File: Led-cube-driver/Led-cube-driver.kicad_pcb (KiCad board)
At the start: 2 copper layers, 31 parts, among them J1 Diodes-input, J2 Vin, J3 Diodes-output, J4 Layers-input, J5 Layers-output, Q1 BC547, Q2 BC547, Q3 BC547, Q4 BC547, U1 74HC164, U2 74HC164

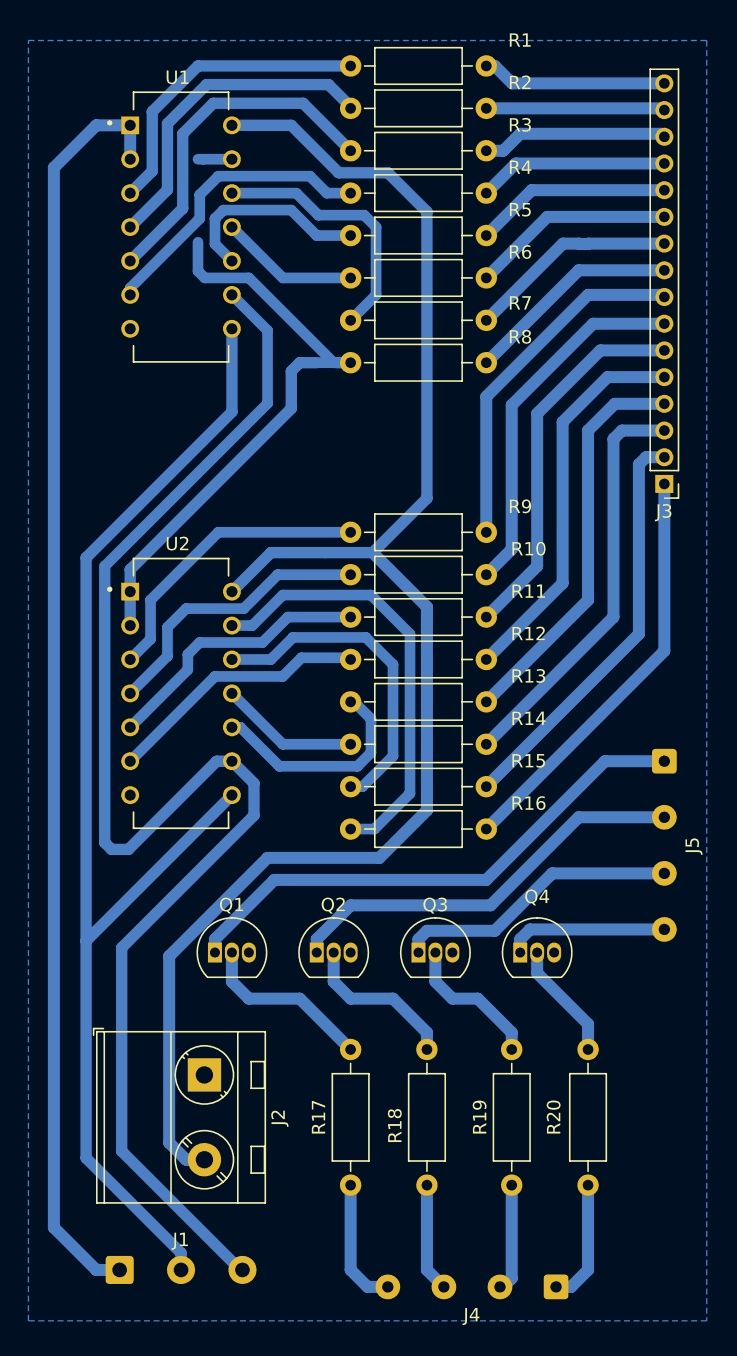
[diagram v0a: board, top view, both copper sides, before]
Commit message: led driver update
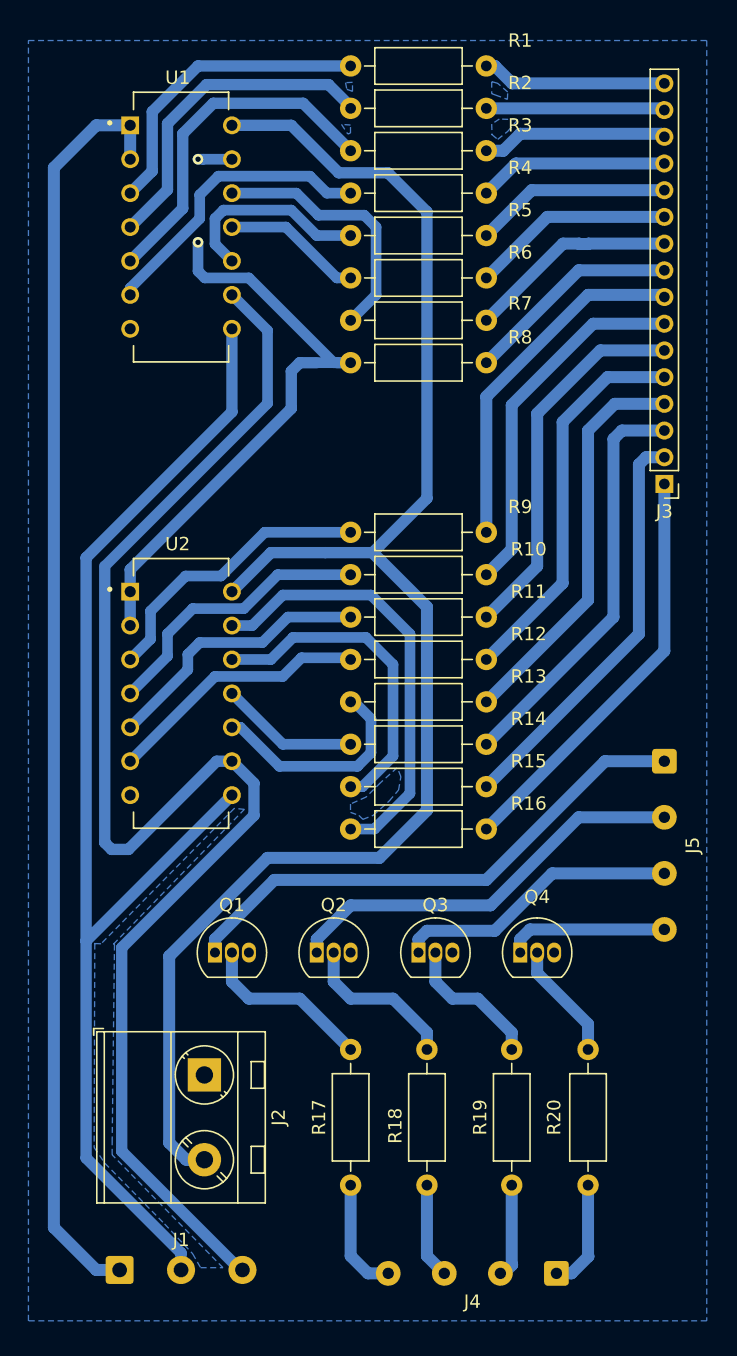
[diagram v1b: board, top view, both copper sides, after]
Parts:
- moved J4 1.02 mm to (131.6, 157.1)
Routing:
- net Net-(J4-Pad1): track 9.27 -> 8.27 mm
- net Net-(J4-Pad4): track 9.66 -> 8.66 mm
- net Net-(J4-Pad3): track 8.15 -> 7.14 mm
- net Net-(J4-Pad2): track 8.13 -> 7.13 mm
- net Net-(R8-Pad1): vias 0 -> 2
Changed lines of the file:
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@@
   )
   (footprint "Connector_Wire:SolderWire-0.25sqmm_1x04_P4.2mm_D0.65mm_OD1.7mm" (layer "F.Cu")
-    (at 131.59 158.115 180)
+    (at 131.62 157.1 180)
     (descr "Soldered wire connection, for 4 times 0.25 mm² wires, basic insulation, conductor diameter 0.65mm, outer diameter 1.7mm, size source Multi-Contact FLEXI-E_0.25 (https://ec.staubli.com/AcroFiles/Catalogues/TM_Cab-Main-11014119_(en)_hi.pdf), bend radius 3 times outer diameter, generated with kicad-footprint-generator")
     (tags "connector wire 0.25sqmm")
@@
   (segment (start 134.016 79.979) (end 139.7 79.979) (width 0.9) (layer "B.Cu") (net 4))
   (segment (start 126.365 85.725) (end 132.111 79.979) (width 0.9) (layer "B.Cu") (net 4))
-  (segment (start 131.59 158.115) (end 132.715 158.115) (width 0.9) (layer "B.Cu") (net 5))
-  (segment (start 133.985 156.845) (end 133.985 150.495) (width 0.9) (layer "B.Cu") (net 5))
-  (segment (start 132.715 158.115) (end 133.985 156.845) (width 0.9) (layer "B.Cu") (net 5))
+  (segment (start 131.62 157.1) (end 132.745 157.1) (width 0.9) (layer "B.Cu") (net 5))
+  (segment (start 134.015 155.83) (end 133.985 155.8) (width 0.9) (layer "B.Cu") (net 5))
+  (segment (start 133.985 155.8) (end 133.985 150.495) (width 0.9) (layer "B.Cu") (net 5))
+  (segment (start 132.745 157.1) (end 134.015 155.83) (width 0.9) (layer "B.Cu") (net 5))
   (segment (start 133.985 140.335) (end 133.985 138.43) (width 0.9) (layer "B.Cu") (net 6))
   (segment (start 133.985 138.43) (end 130.175 134.62) (width 0.9) (layer "B.Cu") (net 6))
   (segment (start 130.175 134.62) (end 130.175 133.075) (width 0.9) (layer "B.Cu") (net 6))
-  (segment (start 128.27 157.48) (end 128.27 150.495) (width 0.9) (layer "B.Cu") (net 7))
-  (segment (start 127.39 158.115) (end 127.635 158.115) (width 0.9) (layer "B.Cu") (net 7))
-  (segment (start 127.635 158.115) (end 128.27 157.48) (width 0.9) (layer "B.Cu") (net 7))
+  (segment (start 128.3 156.465) (end 128.27 156.435) (width 0.9) (layer "B.Cu") (net 7))
+  (segment (start 127.42 157.1) (end 127.665 157.1) (width 0.9) (layer "B.Cu") (net 7))
+  (segment (start 127.665 157.1) (end 128.3 156.465) (width 0.9) (layer "B.Cu") (net 7))
+  (segment (start 128.27 156.435) (end 128.27 150.495) (width 0.9) (layer "B.Cu") (net 7))
   (segment (start 123.825 136.525) (end 122.555 135.255) (width 0.9) (layer "B.Cu") (net 8))
   (segment (start 125.73 136.525) (end 123.825 136.525) (width 0.9) (layer "B.Cu") (net 8))
@@
   (segment (start 122.555 135.255) (end 122.555 133.075) (width 0.9) (layer "B.Cu") (net 8))
   (segment (start 128.27 139.065) (end 125.73 136.525) (width 0.9) (layer "B.Cu") (net 8))
-  (segment (start 121.92 156.845) (end 121.92 150.495) (width 0.9) (layer "B.Cu") (net 9))
-  (segment (start 123.19 158.115) (end 121.92 156.845) (width 0.9) (layer "B.Cu") (net 9))
+  (segment (start 121.92 155.8) (end 121.92 150.495) (width 0.9) (layer "B.Cu") (net 9))
+  (segment (start 123.22 157.1) (end 121.92 155.8) (width 0.9) (layer "B.Cu") (net 9))
   (segment (start 116.205 136.525) (end 114.935 135.255) (width 0.9) (layer "B.Cu") (net 10))
   (segment (start 121.92 139.065) (end 119.38 136.525) (width 0.9) (layer "B.Cu") (net 10))
@@
   (segment (start 121.92 140.335) (end 121.92 139.065) (width 0.9) (layer "B.Cu") (net 10))
   (segment (start 114.935 135.255) (end 114.935 133.075) (width 0.9) (layer "B.Cu") (net 10))
-  (segment (start 117.475 158.115) (end 116.205 156.845) (width 0.9) (layer "B.Cu") (net 11))
-  (segment (start 116.205 156.845) (end 116.205 150.495) (width 0.9) (layer "B.Cu") (net 11))
-  (segment (start 118.99 158.115) (end 117.475 158.115) (width 0.9) (layer "B.Cu") (net 11))
+  (segment (start 116.205 155.8) (end 116.205 150.495) (width 0.9) (layer "B.Cu") (net 11))
+  (segment (start 119.02 157.1) (end 117.505 157.1) (width 0.9) (layer "B.Cu") (net 11))
+  (segment (start 117.505 157.1) (end 116.205 155.8) (width 0.9) (layer "B.Cu") (net 11))
   (segment (start 116.205 140.335) (end 112.395 136.525) (width 0.9) (layer "B.Cu") (net 12))
   (segment (start 112.395 136.525) (end 108.585 136.525) (width 0.9) (layer "B.Cu") (net 12))
@@
   (segment (start 130.175 104.14) (end 130.175 92.71) (width 0.9) (layer "B.Cu") (net 24))
   (segment (start 126.365 107.95) (end 130.175 104.14) (width 0.9) (layer "B.Cu") (net 24))
+  (segment (start 104.38 107.315) (end 108.204 107.315) (width 0.8) (layer "B.Cu") (net 25))
+  (segment (start 102.489 109.206) (end 104.38 107.315) (width 0.8) (layer "B.Cu") (net 25))
+  (segment (start 108.204 107.315) (end 110.744 104.775) (width 0.8) (layer "B.Cu") (net 25))
+  (segment (start 102.489 110.871) (end 102.489 109.206) (width 0.8) (layer "B.Cu") (net 25))
   (segment (start 99.695 113.665) (end 102.489 110.871) (width 0.8) (layer "B.Cu") (net 25))
   (segment (start 110.744 104.775) (end 116.205 104.775) (width 0.8) (layer "B.Cu") (net 25))
-  (segment (start 102.489 110.871) (end 102.489 108.712) (width 0.8) (layer "B.Cu") (net 25))
-  (segment (start 102.489 108.712) (end 103.886 107.315) (width 0.8) (layer "B.Cu") (net 25))
-  (segment (start 103.886 107.315) (end 108.204 107.315) (width 0.8) (layer "B.Cu") (net 25))
-  (segment (start 108.204 107.315) (end 110.744 104.775) (width 0.8) (layer "B.Cu") (net 25))
   (segment (start 128.27 92.075) (end 134.366 85.979) (width 0.9) (layer "B.Cu") (net 26))
   (segment (start 126.365 104.775) (end 128.27 102.87) (width 0.9) (layer "B.Cu") (net 26))
   (segment (start 128.27 102.87) (end 128.27 92.075) (width 0.9) (layer "B.Cu") (net 26))
   (segment (start 134.366 85.979) (end 139.7 85.979) (width 0.9) (layer "B.Cu") (net 26))
+  (segment (start 106.495 104.875) (end 109.77 101.6) (width 0.8) (layer "B.Cu") (net 27))
+  (segment (start 109.77 101.6) (end 116.205 101.6) (width 0.8) (layer "B.Cu") (net 27))
+  (segment (start 103.845 104.875) (end 106.495 104.875) (width 0.8) (layer "B.Cu") (net 27))
   (segment (start 99.695 111.125) (end 101.219 109.601) (width 0.8) (layer "B.Cu") (net 27))
-  (segment (start 101.219 106.68) (end 106.299 101.6) (width 0.8) (layer "B.Cu") (net 27))
-  (segment (start 106.299 101.6) (end 116.205 101.6) (width 0.8) (layer "B.Cu") (net 27))
-  (segment (start 101.219 109.601) (end 101.219 106.68) (width 0.8) (layer "B.Cu") (net 27))
+  (segment (start 101.219 107.501) (end 103.845 104.875) (width 0.8) (layer "B.Cu") (net 27))
+  (segment (start 101.219 109.601) (end 101.219 107.501) (width 0.8) (layer "B.Cu") (net 27))
   (segment (start 133.985 83.82) (end 139.541 83.82) (width 0.9) (layer "B.Cu") (net 28))
   (segment (start 139.541 83.82) (end 139.7 83.979) (width 0.9) (layer "B.Cu") (net 28))
   (segment (start 126.365 101.6) (end 126.365 91.44) (width 0.9) (layer "B.Cu") (net 28))
   (segment (start 126.365 91.44) (end 133.985 83.82) (width 0.9) (layer "B.Cu") (net 28))
+  (via (at 104.775 73.66) (size 0.8) (drill 0.4) (layers "F.Cu" "B.Cu") (net 29))
+  (via (at 104.775 79.883) (size 0.8) (drill 0.4) (layers "F.Cu" "B.Cu") (net 29))
   (segment (start 115.189 88.9) (end 116.205 88.9) (width 0.85) (layer "B.Cu") (net 29))
   (segment (start 104.775 82.042) (end 104.775 79.883) (width 0.8) (layer "B.Cu") (net 29))
@@
   (segment (start 133.286 81.979) (end 139.7 81.979) (width 0.9) (layer "B.Cu") (net 30))
   (segment (start 126.365 88.9) (end 133.286 81.979) (width 0.9) (layer "B.Cu") (net 30))
-  (segment (start 111.125 82.55) (end 116.205 82.55) (width 0.8) (layer "B.Cu") (net 31))
-  (segment (start 107.315 78.74) (end 111.125 82.55) (width 0.8) (layer "B.Cu") (net 31))
+  (segment (start 115.17 82.55) (end 116.205 82.55) (width 0.8) (layer "B.Cu") (net 31))
+  (segment (start 111.36 78.74) (end 115.17 82.55) (width 0.8) (layer "B.Cu") (net 31))
+  (segment (start 107.315 78.74) (end 111.36 78.74) (width 0.8) (layer "B.Cu") (net 31))
   (segment (start 126.365 82.55) (end 130.936 77.979) (width 0.9) (layer "B.Cu") (net 32))
   (segment (start 130.936 77.979) (end 139.7 77.979) (width 0.9) (layer "B.Cu") (net 32))
@@
       )
     )
+    (polygon
+      (pts
+        (xy 97.514638 132.416488)
+        (xy 97.044916 132.400831)
+        (xy 97.045 132.375)
+        (xy 97.02 132.4)
+        (xy 97.044916 132.400831)
+        (xy 96.995 147.675)
+        (xy 97.795 148.85)
+        (xy 102.27 153.4)
+        (xy 104.37 155.625)
+        (xy 104.97 156.675)
+        (xy 106.645 156.675)
+        (xy 98.345 148.225)
+        (xy 98.345 147.3)
+        (xy 98.52 132.45)
+        (xy 98.441708 132.44739)
+        (xy 108.245 122.35)
+        (xy 107.495 122.275)
+      )
+    )
+    (polygon
+      (pts
+        (xy 118.445 120.35)
+        (xy 117.37 121.425)
+        (xy 116.195 121.95)
+        (xy 116.195 122.575)
+        (xy 116.82 122.8)
+        (xy 117.12 123.1)
+        (xy 117.895 122.8)
+        (xy 119.095 121.725)
+        (xy 119.795 120.9)
+        (xy 119.97 119.9)
+        (xy 119.695 119.225)
+      )
+    )
+    (polygon
+      (pts
+        (xy 126.77 71.025)
+        (xy 126.794219 71.8)
+        (xy 126.77 71.8)
+        (xy 126.794866 71.820722)
+        (xy 126.795 71.825)
+        (xy 126.795 71.820833)
+        (xy 127.22 72.175)
+        (xy 127.97 71.575)
+        (xy 128.72 70.7)
+        (xy 127.345 70.65)
+      )
+    )
+    (polygon
+      (pts
+        (xy 115.995 71.775)
+        (xy 116.195 71.7)
+        (xy 116.195 71.1)
+        (xy 115.52 71.05)
+      )
+    )
+    (polygon
+      (pts
+        (xy 126.77 68.75)
+        (xy 127.045 68.85)
+        (xy 127.945 69.175)
+        (xy 127.97 68.625)
+        (xy 127.22 67.975)
+        (xy 126.77 67.85)
+      )
+    )
+    (polygon
+      (pts
+        (xy 115.82 67.925)
+        (xy 115.92 68.425)
+        (xy 116.345 68.575)
+        (xy 116.345 67.9)
+      )
+    )

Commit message: done
done
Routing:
- net Net-(J1-Pad2): track 93.4 -> 94.3 mm
- net Net-(J1-Pad3): track 106.4 -> 105.5 mm
- net Net-(R8-Pad1): track 47.7 -> 47.0 mm
- net Net-(J1-Pad1): track 95.2 -> 95.7 mm

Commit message: newFiles
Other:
- board outline added: 51.2 x 96.1 mm
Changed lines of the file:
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@@
     (pad "14" thru_hole circle (at 3.81 -7.62) (size 1.338 1.338) (drill 0.83) (layers *.Cu *.Mask)
       (net 2 "VCC") (pinfunction "VCC") (pintype "power_in"))
+    (model "C:/Users/domin/Downloads/HEF4071BP.STEP"
+      (offset (xyz 0 0 0))
+      (scale (xyz 1 1 1))
+      (rotate (xyz -90 0 0))
+    )
   )
   (footprint "Package_TO_SOT_THT:TO-92_Inline" (layer "F.Cu")
@@
     (pad "2" thru_hole circle (at 6.35 0 270) (size 2.5 2.5) (drill 1.3) (layers *.Cu *.Mask)
       (net 2 "VCC") (pinfunction "Pin_2") (pintype "passive"))
-    (model "${KICAD6_3DMODEL_DIR}/TerminalBlock_MetzConnect.3dshapes/TerminalBlock_MetzConnect_Type701_RT11L02HGLU_1x02_P6.35mm_Horizontal.wrl"
-      (offset (xyz 0 0 0))
-      (scale (xyz 1 1 1))
-      (rotate (xyz 0 0 0))
-    )
   )
   (footprint "Connector_Wire:SolderWire-0.25sqmm_1x04_P4.2mm_D0.65mm_OD1.7mm" (layer "F.Cu")
@@
     (pad "14" thru_hole circle (at 3.81 -7.62) (size 1.338 1.338) (drill 0.83) (layers *.Cu *.Mask)
       (net 2 "VCC") (pinfunction "VCC") (pintype "power_in"))
+    (model "C:/Users/domin/Downloads/HEF4071BP.STEP"
+      (offset (xyz 0 0 0))
+      (scale (xyz 1 1 1))
+      (rotate (xyz -90 0 0))
+    )
   )
   (footprint "Resistor_THT:R_Axial_DIN0207_L6.3mm_D2.5mm_P10.16mm_Horizontal" (layer "F.Cu")
@@
     )
   )
+  (gr_rect (start 91.97 64.65) (end 143.145 160.75) (layer "Edge.Cuts") (width 0.05) (fill none))
   (segment (start 99.4194 121.285) (end 99.695 121.285) (width 0.25) (layer "B.Cu") (net 1))
   (segment (start 103.886 148.59) (end 102.616 147.32) (width 0.9) (layer "B.Cu") (net 2))
